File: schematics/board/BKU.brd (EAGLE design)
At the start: 94 x 94 mm, 75 parts

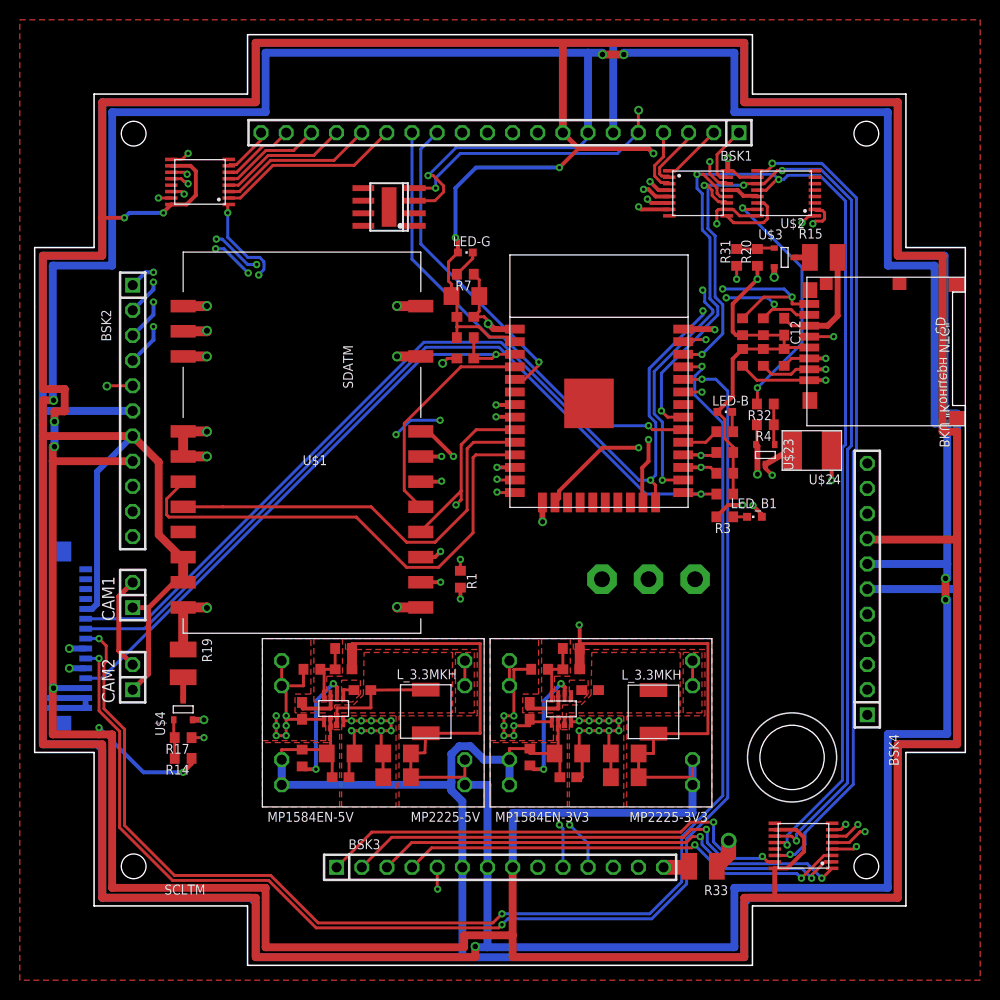
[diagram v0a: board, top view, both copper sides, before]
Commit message: Добавлена шелкографика на плате БКУ
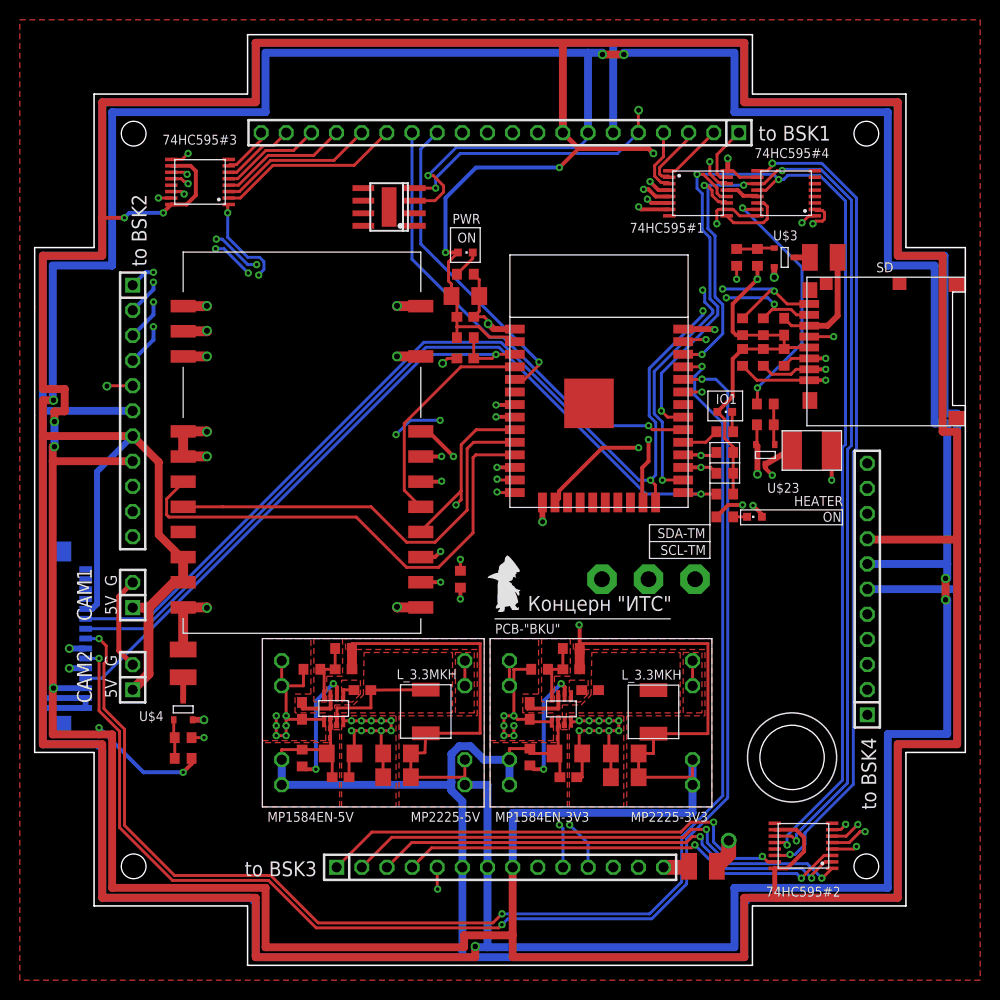
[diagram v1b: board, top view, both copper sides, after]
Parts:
- added 74HC595#4: 74HC595, CanCubeSat:TSSOP16
- added U$6: PCB-"BKU", CanCubeSat:ITS-LOGO
- U$2: value 74HC595 -> PCB-"BKU"; device CanCubeSat:TSSOP16 -> CanCubeSat:ITS-LOGO
- moved U$2 52.1 mm to (46.5, 35.0), turned to 0 degrees
- renumbered U$18 to 74HC595#1, U$19 to 74HC595#2, U$20 to 74HC595#3
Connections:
- net 3V3: now also 74HC595#4.10, 74HC595#4.16; no longer U$2.10, U$2.16
- net BKU-KHEAT: now also 74HC595#4.15; no longer U$2.15
- net CS-SR: now also 74HC595#4.12; no longer U$2.12
- net GND: now also 74HC595#4.13, 74HC595#4.8; no longer U$2.13, U$2.8
- net N$1: now also 74HC595#4.14; no longer U$2.14
- net N$7: now also 74HC595#4.9; no longer U$2.9
- net RADIO: now also 74HC595#4.2; no longer U$2.2
- net SCK: now also 74HC595#4.11; no longer U$2.11
- net SD: now also 74HC595#4.1; no longer U$2.1
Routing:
- net DAT1: track 42.3 -> 40.3 mm
- net 3V3: track 659.6 -> 661.1 mm
- net GND-OUT: track 603.5 -> 602.6 mm
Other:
- board text added: "5V"
- board text added: "ARK POWER"
- board text added: "G"
- board text added: "HEATER"
- board text added: "IO1"
- board text added: "ON"
- board text added: "PWR"
- board text added: "SCL-TM"
- board text added: "SDA-TM"
- board text added: "for firmware"
- board text added: "to BSK1"
- board text added: "to BSK2"
- board text added: "to BSK3"
- board text added: "to BSK4"
- board text removed: "BKU "Концерн ИТС""
- board text removed: "SCLTM"
- board text removed: "SDATM"

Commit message: Убран лишний переключатель на плате БКУ
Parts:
- removed S1: (no value), cansat-lib:UNICS-SWITCH
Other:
- board text removed: "ARK POWER"
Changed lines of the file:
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@@
 <grid distance="0.5" unitdist="mm" unit="mm" style="lines" multiple="1" display="yes" altdistance="0.1" altunitdist="mm" altunit="mm"/>
 <layers>
-<layer number="1" name="Top" color="4" fill="1" visible="yes" active="yes"/>
-<layer number="2" name="Route2" color="16" fill="1" visible="yes" active="yes"/>
+<layer number="1" name="Top" color="4" fill="1" visible="no" active="yes"/>
+<layer number="2" name="Route2" color="16" fill="1" visible="no" active="yes"/>
 <layer number="3" name="Route3" color="17" fill="1" visible="no" active="no"/>
 <layer number="4" name="Route4" color="18" fill="1" visible="no" active="no"/>
@@
 <layer number="13" name="Route13" color="21" fill="1" visible="no" active="no"/>
 <layer number="14" name="Route14" color="22" fill="1" visible="no" active="no"/>
-<layer number="15" name="Route15" color="23" fill="1" visible="yes" active="yes"/>
+<layer number="15" name="Route15" color="23" fill="1" visible="no" active="yes"/>
 <layer number="16" name="Bottom" color="1" fill="1" visible="yes" active="yes"/>
 <layer number="17" name="Pads" color="2" fill="1" visible="yes" active="yes"/>
@@
 <layer number="19" name="Unrouted" color="6" fill="1" visible="yes" active="yes"/>
 <layer number="20" name="Dimension" color="24" fill="1" visible="yes" active="yes"/>
-<layer number="21" name="tPlace" color="7" fill="1" visible="yes" active="yes"/>
+<layer number="21" name="tPlace" color="7" fill="1" visible="no" active="yes"/>
 <layer number="22" name="bPlace" color="7" fill="1" visible="yes" active="yes"/>
-<layer number="23" name="tOrigins" color="15" fill="1" visible="yes" active="yes"/>
+<layer number="23" name="tOrigins" color="15" fill="1" visible="no" active="yes"/>
 <layer number="24" name="bOrigins" color="15" fill="1" visible="yes" active="yes"/>
-<layer number="25" name="tNames" color="7" fill="1" visible="yes" active="yes"/>
+<layer number="25" name="tNames" color="7" fill="1" visible="no" active="yes"/>
 <layer number="26" name="bNames" color="7" fill="1" visible="yes" active="yes"/>
 <layer number="27" name="tValues" color="7" fill="1" visible="no" active="yes"/>
@@
 <layer number="37" name="tTest" color="7" fill="1" visible="no" active="yes"/>
 <layer number="38" name="bTest" color="7" fill="1" visible="no" active="yes"/>
-<layer number="39" name="tKeepout" color="4" fill="11" visible="yes" active="yes"/>
+<layer number="39" name="tKeepout" color="4" fill="11" visible="no" active="yes"/>
 <layer number="40" name="bKeepout" color="1" fill="11" visible="yes" active="yes"/>
-<layer number="41" name="tRestrict" color="4" fill="10" visible="yes" active="yes"/>
+<layer number="41" name="tRestrict" color="4" fill="10" visible="no" active="yes"/>
 <layer number="42" name="bRestrict" color="1" fill="10" visible="yes" active="yes"/>
 <layer number="43" name="vRestrict" color="2" fill="10" visible="no" active="yes"/>
@@
 <layer number="49" name="Reference" color="7" fill="1" visible="no" active="yes"/>
 <layer number="50" name="dxf" color="7" fill="1" visible="no" active="yes"/>
-<layer number="51" name="tDocu" color="7" fill="1" visible="yes" active="yes"/>
+<layer number="51" name="tDocu" color="7" fill="1" visible="no" active="yes"/>
 <layer number="52" name="bDocu" color="7" fill="1" visible="yes" active="yes"/>
 <layer number="53" name="tGND_GNDA" color="7" fill="9" visible="no" active="no"/>
@@
 <text x="4.3" y="46.7" size="1.2" layer="22" ratio="20" rot="MR180" align="bottom-center">for
 firmware</text>
-<text x="67.5" y="43" size="1.5" layer="22" ratio="20" rot="MR0">ARK POWER</text>
 </plain>
 <attributes>
@@
 <attribute name="VALUE" x="13.075" y="26.56" size="1.27" layer="27" rot="R90"/>
 </element>
-<element name="S1" library="cansat-lib" package="UNICS-SWITCH" package3d_urn="urn:adsk.eagle:package:27679/1" value="" x="62" y="39" smashed="yes" rot="MR0">
-<attribute name="VALUE" x="62" y="42.556" size="1.27" layer="28" ratio="10" rot="MR0"/>
-</element>
 <element name="U$2" library="CanCubeSat" package="ITS-LOGO" value="PCB-&quot;BKU&quot;" x="46.5" y="35" smashed="yes">

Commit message: Добавлены герберы плат BKU и Debug
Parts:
- moved R10 1.00 mm to (70.7, 49.7)
- moved R11 1.00 mm to (70.7, 51.8)
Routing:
- net 1W: track 372.3 -> 375.9 mm
- net SCK: track 201.3 -> 204.1 mm
- net GND: track 203.3 -> 201.0 mm
- net MOSI: track 78.4 -> 80.5 mm
- net EN: track 61.4 -> 59.7 mm
- net TX-E: track 140.7 -> 142.4 mm
- net MTDI: track 52.6 -> 53.8 mm
- net MTMS: track 50.7 -> 51.9 mm
- net CS-RA: track 38.6 -> 39.8 mm
- net IO0-E: track 83.5 -> 84.5 mm
- net 3V3: track 661.1 -> 662.1 mm
- net SCL-TM: track 283.4 -> 284.2 mm
- net DIO1: track 22.9 -> 22.2 mm
- net TX-EN: track 42.8 -> 42.0 mm
- net TIME-ES: track 32.1 -> 32.9 mm
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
